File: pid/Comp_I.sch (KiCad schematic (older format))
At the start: 23 parts, among them U10 LM7171, U9 LM7171

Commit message: [pid] -
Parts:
- removed C40, C43: 2n, ~, symbol C
- removed R30, R35: 500, ~, symbol R
- removed R32, R34: 50, ~, symbol R
- added C29: 10u, ~, symbol C
- added C30: 0.01u, ~, symbol C
- added R49: 200k, ~, symbol R
- added R51: 0, ~, symbol R
- added R54: 1M, ~, symbol R
- added R56: 510, ~, symbol R
- added RV14: 100k, ~, symbol POT
- gave numbers to parts that had none: 4
- renumbered C36 to C21, C37 to C22, C38 to C23, C39 to C24, C41 to C27, C42 to C28, R31 to R47, R33 to R50, R36 to R53, R37 to R55, RV3 to RV15, U9 to U5, U10 to U6
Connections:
- net +5V: now also RV14.1
- net -5V: now also RV14.3
- net GND: now also C29.2, C30.1, R54.2
- net Out: now also R56.1
- net at R53.1, U5.6 (Out), U6.2 (-In): now also R51.2
- net Switch_NC/NC renamed Hold/NC
- net Switch_NO/NO renamed Reset1/NO
- net Reset1/NO: now also R49.2, R51.1
- new net: C29.1, R49.1, RV14.2
- new net Reset1/COM: C30.2, R54.1
- new net Reset2/COM: R56.2

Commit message: [pid] -
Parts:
- renumbered R47 to R50, R48 to R51, R49 to R52, R50 to R53, R51 to R54, R52 to R55, R53 to R56, R54 to R57, R55 to R58, R56 to R59
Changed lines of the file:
@@
 $Descr A4 11693 8268
 encoding utf-8
-Sheet 10 47
+Sheet 10 53
 Title ""
-Date "1 may 2014"
+Date "2 may 2014"
 Rev ""
 Comp ""
@@
 	3000 3400 3200 3400
 $Comp
-L R R47
+L R R50
 U 1 1 531FD1A4
 P 4950 3100
-F 0 "R47" V 5030 3100 40  0000 C CNN
+F 0 "R50" V 5030 3100 40  0000 C CNN
 F 1 "100" V 4957 3101 40  0000 C CNN
 F 2 "~" V 4880 3100 30  0000 C CNN
@@
 	7850 3750 7900 3750
 $Comp
-L GND #PWR026
+L GND #PWR031
 U 1 1 531FD1D3
 P 7300 3500
-F 0 "#PWR026" H 7300 3500 30  0001 C CNN
+F 0 "#PWR031" H 7300 3500 30  0001 C CNN
 F 1 "GND" H 7300 3430 30  0001 C CNN
 F 2 "" H 7300 3500 60  0000 C CNN
@@
 	7300 3400 7300 3500
 $Comp
-L R R55
+L R R58
 U 1 1 531FD1DB
 P 8400 2950
-F 0 "R55" V 8480 2950 40  0000 C CNN
+F 0 "R58" V 8480 2950 40  0000 C CNN
 F 1 "200" V 8407 2951 40  0000 C CNN
 F 2 "~" V 8330 2950 30  0000 C CNN
@@
 	8400 2650 8400 2700
 $Comp
-L GND #PWR027
+L GND #PWR032
 U 1 1 531FD1E9
 P 8600 2200
-F 0 "#PWR027" H 8600 2200 30  0001 C CNN
+F 0 "#PWR032" H 8600 2200 30  0001 C CNN
 F 1 "GND" H 8600 2130 30  0001 C CNN
 F 2 "" H 8600 2200 60  0000 C CNN
@@
 $EndComp
 $Comp
-L GND #PWR028
+L GND #PWR033
 U 1 1 531FD20B
 P 2550 1450
-F 0 "#PWR028" H 2550 1450 30  0001 C CNN
+F 0 "#PWR033" H 2550 1450 30  0001 C CNN
 F 1 "GND" H 2550 1380 30  0001 C CNN
 F 2 "" H 2550 1450 60  0000 C CNN
@@
 $Sheet
 S 7400 4050 600  350
-U 5321AFC9
+U 5364DD9B
 F0 "Reset2" 50
 F1 "Switch_NO.sch" 50
@@
 $EndComp
 $Comp
-L GND #PWR029
+L GND #PWR034
 U 1 1 531FF000
 P 5900 4600
-F 0 "#PWR029" H 5900 4600 30  0001 C CNN
+F 0 "#PWR034" H 5900 4600 30  0001 C CNN
 F 1 "GND" H 5900 4530 30  0001 C CNN
 F 2 "" H 5900 4600 60  0000 C CNN
@@
 	7200 3200 7350 3200
 $Comp
-L R R53
+L R R56
 U 1 1 531FF15A
 P 7200 3650
-F 0 "R53" V 7280 3650 40  0000 C CNN
+F 0 "R56" V 7280 3650 40  0000 C CNN
 F 1 "510" V 7207 3651 40  0000 C CNN
 F 2 "~" V 7130 3650 30  0000 C CNN
@@
 	7200 2600 7200 3400
 $Comp
-L R R50
+L R R53
 U 1 1 531FF1DB
 P 6100 3550
-F 0 "R50" V 6180 3550 40  0000 C CNN
+F 0 "R53" V 6180 3550 40  0000 C CNN
 F 1 "10" V 6107 3551 40  0000 C CNN
 F 2 "~" V 6030 3550 30  0000 C CNN
@@
 $EndComp
 $Comp
-L GND #PWR030
+L GND #PWR035
 U 1 1 531FF1E1
 P 6100 4050
-F 0 "#PWR030" H 6100 4050 30  0001 C CNN
+F 0 "#PWR035" H 6100 4050 30  0001 C CNN
 F 1 "GND" H 6100 3980 30  0001 C CNN
 F 2 "" H 6100 4050 60  0000 C CNN
@@
 Connection ~ 5900 4150
 $Comp
-L R R48
+L R R51
 U 1 1 5355E970
 P 5550 3100
-F 0 "R48" V 5630 3100 40  0000 C CNN
+F 0 "R51" V 5630 3100 40  0000 C CNN
 F 1 "10" V 5557 3101 40  0000 C CNN
 F 2 "~" V 5480 3100 30  0000 C CNN
@@
 $EndComp
 $Comp
-L R R52
+L R R55
 U 1 1 5355E9CA
 P 6800 2400
-F 0 "R52" V 6880 2400 40  0000 C CNN
+F 0 "R55" V 6880 2400 40  0000 C CNN
 F 1 "100" V 6807 2401 40  0000 C CNN
 F 2 "~" V 6730 2400 30  0000 C CNN
@@
 Connection ~ 5250 3100
 $Comp
-L GND #PWR031
+L GND #PWR036
 U 1 1 5355EE90
 P 5250 3650
-F 0 "#PWR031" H 5250 3650 30  0001 C CNN
+F 0 "#PWR036" H 5250 3650 30  0001 C CNN
 F 1 "GND" H 5250 3580 30  0001 C CNN
 F 2 "" H 5250 3650 60  0000 C CNN
@@
 $EndComp
 $Comp
-L R R49
+L R R52
 U 1 1 5356CEAF
 P 5900 2150
-F 0 "R49" V 5980 2150 40  0000 C CNN
+F 0 "R52" V 5980 2150 40  0000 C CNN
 F 1 "200k" V 5907 2151 40  0000 C CNN
 F 2 "~" V 5830 2150 30  0000 C CNN
@@
 $EndComp
 $Comp
-L GND #PWR032
+L GND #PWR037
 U 1 1 5356D867
 P 6450 1950
-F 0 "#PWR032" H 6450 1950 30  0001 C CNN
+F 0 "#PWR037" H 6450 1950 30  0001 C CNN
 F 1 "GND" H 6450 1880 30  0001 C CNN
 F 2 "" H 6450 1950 60  0000 C CNN
@@
 	6450 1850 6450 1950
 $Comp
-L R R51
+L R R54
 U 1 1 5358064E
 P 6600 2600
-F 0 "R51" V 6680 2600 40  0000 C CNN
+F 0 "R54" V 6680 2600 40  0000 C CNN
 F 1 "0" V 6607 2601 40  0000 C CNN
 F 2 "~" V 6530 2600 30  0000 C CNN
@@
 $EndComp
 $Comp
-L GND #PWR033
+L GND #PWR038
 U 1 1 535811B7
 P 7050 4900
-F 0 "#PWR033" H 7050 4900 30  0001 C CNN
+F 0 "#PWR038" H 7050 4900 30  0001 C CNN
 F 1 "GND" H 7050 4830 30  0001 C CNN
 F 2 "" H 7050 4900 60  0000 C CNN
@@
 Connection ~ 6200 5000
 $Comp
-L R R56
+L R R59
 U 1 1 535829AC
 P 8400 3700
-F 0 "R56" V 8480 3700 40  0000 C CNN
+F 0 "R59" V 8480 3700 40  0000 C CNN
 F 1 "510" V 8407 3701 40  0000 C CNN
 F 2 "~" V 8330 3700 30  0000 C CNN
@@
 	8400 3950 8400 4150
 $Comp
-L R R54
+L R R57
 U 1 1 53583740
 P 7200 4550
-F 0 "R54" V 7280 4550 40  0000 C CNN
+F 0 "R57" V 7280 4550 40  0000 C CNN
 F 1 "1M" V 7207 4551 40  0000 C CNN
 F 2 "~" V 7130 4550 30  0000 C CNN

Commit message: [pid] layout
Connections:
- net Reset1/COM: now also C27.1, C28.2, R51.2, R52.2, R54.1, U5.3 (+In); no longer C30.2, R57.1
- net Reset1/NO: now also C30.2, R57.1; no longer C27.1, C28.2, R51.2, R52.2, R54.1, U5.3 (+In)
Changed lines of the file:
@@
 Sheet 10 53
 Title ""
-Date "2 may 2014"
+Date "5 may 2014"
 Rev ""
 Comp ""
@@
 	7850 3750 7900 3750
 $Comp
-L GND #PWR42
+L GND #PWR036
 U 1 1 531FD1D3
 P 7300 3500
-F 0 "#PWR42" H 7300 3500 30  0001 C CNN
+F 0 "#PWR036" H 7300 3500 30  0001 C CNN
 F 1 "GND" H 7300 3430 30  0001 C CNN
 F 2 "" H 7300 3500 60  0000 C CNN
@@
 	8400 2650 8400 2700
 $Comp
-L GND #PWR43
+L GND #PWR037
 U 1 1 531FD1E9
 P 8600 2200
-F 0 "#PWR43" H 8600 2200 30  0001 C CNN
+F 0 "#PWR037" H 8600 2200 30  0001 C CNN
 F 1 "GND" H 8600 2130 30  0001 C CNN
 F 2 "" H 8600 2200 60  0000 C CNN
@@
 $EndComp
 $Comp
-L GND #PWR36
+L GND #PWR038
 U 1 1 531FD20B
 P 2550 1450
-F 0 "#PWR36" H 2550 1450 30  0001 C CNN
+F 0 "#PWR038" H 2550 1450 30  0001 C CNN
 F 1 "GND" H 2550 1380 30  0001 C CNN
 F 2 "" H 2550 1450 60  0000 C CNN
@@
 $EndComp
 $Comp
-L GND #PWR38
+L GND #PWR039
 U 1 1 531FF000
 P 5900 4600
-F 0 "#PWR38" H 5900 4600 30  0001 C CNN
+F 0 "#PWR039" H 5900 4600 30  0001 C CNN
 F 1 "GND" H 5900 4530 30  0001 C CNN
 F 2 "" H 5900 4600 60  0000 C CNN
@@
 $EndComp
 $Comp
-L GND #PWR39
+L GND #PWR040
 U 1 1 531FF1E1
 P 6100 4050
-F 0 "#PWR39" H 6100 4050 30  0001 C CNN
+F 0 "#PWR040" H 6100 4050 30  0001 C CNN
 F 1 "GND" H 6100 3980 30  0001 C CNN
 F 2 "" H 6100 4050 60  0000 C CNN
@@
 Connection ~ 5250 3100
 $Comp
-L GND #PWR37
+L GND #PWR041
 U 1 1 5355EE90
 P 5250 3650
-F 0 "#PWR37" H 5250 3650 30  0001 C CNN
+F 0 "#PWR041" H 5250 3650 30  0001 C CNN
 F 1 "GND" H 5250 3580 30  0001 C CNN
 F 2 "" H 5250 3650 60  0000 C CNN
@@
 $EndComp
 $Comp
-L GND #PWR40
+L GND #PWR042
 U 1 1 5356D867
 P 6450 1950
-F 0 "#PWR40" H 6450 1950 30  0001 C CNN
+F 0 "#PWR042" H 6450 1950 30  0001 C CNN
 F 1 "GND" H 6450 1880 30  0001 C CNN
 F 2 "" H 6450 1950 60  0000 C CNN
@@
 F0 "Reset1" 50
 F1 "Switch_NO.sch" 50
-F2 "NO" I L 6300 4150 60
+F2 "NO" I R 6900 4150 60
 F3 "IN" I L 6300 4300 60
-F4 "COM" I R 6900 4150 60
+F4 "COM" I L 6300 4150 60
 $EndSheet
 $Comp
@@
 $EndComp
 $Comp
-L GND #PWR41
+L GND #PWR043
 U 1 1 535811B7
 P 7050 4900
-F 0 "#PWR41" H 7050 4900 30  0001 C CNN
+F 0 "#PWR043" H 7050 4900 30  0001 C CNN
 F 1 "GND" H 7050 4830 30  0001 C CNN
 F 2 "" H 7050 4900 60  0000 C CNN

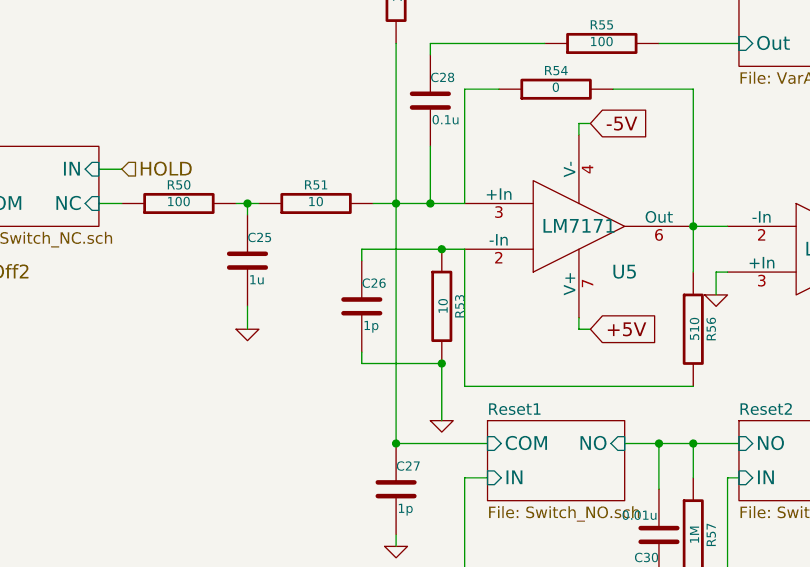
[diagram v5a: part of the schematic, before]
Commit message: [pid] remove high freq bypass capacitor for integrator pre amp
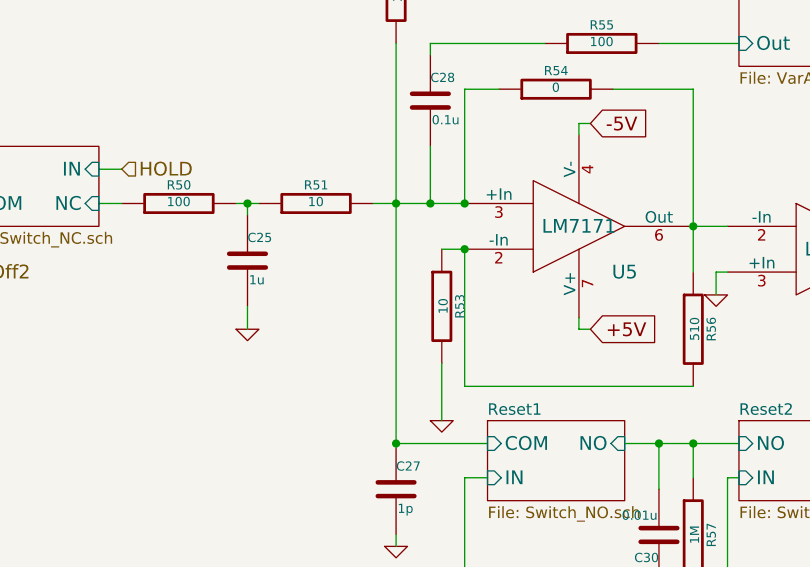
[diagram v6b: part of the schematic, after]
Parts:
- removed C26: 1p, ~, symbol C
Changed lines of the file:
@@
 Sheet 10 53
 Title ""
-Date "5 may 2014"
+Date "19 may 2014"
 Rev ""
 Comp ""
@@
 	6200 3900 6200 3300
 Wire Wire Line
-	6200 3300 5750 3300
-Wire Wire Line
 	6100 3800 6100 4050
 Wire Wire Line
 	8350 3300 8450 3300
 Connection ~ 8400 3300
-$Comp
-L C C26
-U 1 1 53558A6B
-P 5750 3550
-F 0 "C26" H 5750 3650 40  0000 L CNN
-F 1 "1p" H 5756 3465 40  0000 L CNN
-F 2 "~" H 5788 3400 30  0000 C CNN
-F 3 "~" H 5750 3550 60  0000 C CNN
-	1    5750 3550
-	1    0    0    -1
-$EndComp
-Wire Wire Line
-	5750 3300 5750 3350
-Connection ~ 6100 3300
-Wire Wire Line
-	5750 3750 5750 3800
-Wire Wire Line
-	5750 3800 6100 3800
-Connection ~ 6100 3800
 Connection ~ 5900 3100
 Connection ~ 5900 4150
@@
 Wire Wire Line
 	4600 2950 4700 2950
+Wire Wire Line
+	6200 3300 6100 3300
+Connection ~ 6200 3300
+Connection ~ 6200 3100
 $EndSCHEMATC

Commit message: [pid] update
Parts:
- C27: value 1p -> 0(1p)
- C28: value 0.1u -> 0.022u
- C30: value 0.01u -> 10u
- R50: value 100 -> 5k
- R51: value 10 -> 5
- R53: value 10 -> 100
- R54: value 0 -> inf(0)
- R55: value 100 -> 200
- R57: value 1M -> 1k
- R59: value 510 -> 1k
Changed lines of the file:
@@
 Sheet 10 53
 Title ""
-Date "19 may 2014"
+Date "28 may 2014"
 Rev ""
 Comp ""
@@
 P 4950 3100
 F 0 "R50" V 5030 3100 40  0000 C CNN
-F 1 "100" V 4957 3101 40  0000 C CNN
+F 1 "5k" V 4957 3101 40  0000 C CNN
 F 2 "~" V 4880 3100 30  0000 C CNN
 F 3 "~" H 4950 3100 30  0000 C CNN
@@
 F 3 "~" H 7750 3300 60  0000 C CNN
 	1    7750 3300
-	1    0    0    -1
-$EndComp
-$Comp
-L C C28
-U 1 1 531FD1B0
-P 6050 2650
-F 0 "C28" H 6050 2750 40  0000 L CNN
-F 1 "0.1u" H 6056 2565 40  0000 L CNN
-F 2 "~" H 6088 2500 30  0000 C CNN
-F 3 "~" H 6050 2650 60  0000 C CNN
-	1    6050 2650
 	1    0    0    -1
 $EndComp
@@
 P 5900 4350
 F 0 "C27" H 5900 4450 40  0000 L CNN
-F 1 "1p" H 5906 4265 40  0000 L CNN
+F 1 "0(1p)" H 5906 4265 40  0000 L CNN
 F 2 "~" H 5938 4200 30  0000 C CNN
 F 3 "~" H 5900 4350 60  0000 C CNN
@@
 P 6100 3550
 F 0 "R53" V 6180 3550 40  0000 C CNN
-F 1 "10" V 6107 3551 40  0000 C CNN
+F 1 "100" V 6107 3551 40  0000 C CNN
 F 2 "~" V 6030 3550 30  0000 C CNN
 F 3 "~" H 6100 3550 30  0000 C CNN
@@
 P 5550 3100
 F 0 "R51" V 5630 3100 40  0000 C CNN
-F 1 "10" V 5557 3101 40  0000 C CNN
+F 1 "5" V 5557 3101 40  0000 C CNN
 F 2 "~" V 5480 3100 30  0000 C CNN
 F 3 "~" H 5550 3100 30  0000 C CNN
@@
 P 6800 2400
 F 0 "R55" V 6880 2400 40  0000 C CNN
-F 1 "100" V 6807 2401 40  0000 C CNN
+F 1 "200" V 6807 2401 40  0000 C CNN
 F 2 "~" V 6730 2400 30  0000 C CNN
 F 3 "~" H 6800 2400 30  0000 C CNN
@@
 P 6600 2600
 F 0 "R54" V 6680 2600 40  0000 C CNN
-F 1 "0" V 6607 2601 40  0000 C CNN
+F 1 "inf(0)" V 6607 2601 40  0000 C CNN
 F 2 "~" V 6530 2600 30  0000 C CNN
 F 3 "~" H 6600 2600 30  0000 C CNN
@@
 P 7050 4550
 F 0 "C30" H 7050 4650 40  0000 L CNN
-F 1 "0.01u" H 7056 4465 40  0000 L CNN
+F 1 "10u" H 7056 4465 40  0000 L CNN
 F 2 "~" H 7088 4400 30  0000 C CNN
 F 3 "~" H 7050 4550 60  0000 C CNN
@@
 P 8400 3700
 F 0 "R59" V 8480 3700 40  0000 C CNN
-F 1 "510" V 8407 3701 40  0000 C CNN
+F 1 "1k" V 8407 3701 40  0000 C CNN
 F 2 "~" V 8330 3700 30  0000 C CNN
 F 3 "~" H 8400 3700 30  0000 C CNN
@@
 P 7200 4550
 F 0 "R57" V 7280 4550 40  0000 C CNN
-F 1 "1M" V 7207 4551 40  0000 C CNN
+F 1 "1k" V 7207 4551 40  0000 C CNN
 F 2 "~" V 7130 4550 30  0000 C CNN
 F 3 "~" H 7200 4550 30  0000 C CNN
@@
 Connection ~ 6200 3300
 Connection ~ 6200 3100
+$Comp
+L C C28
+U 1 1 531FD1B0
+P 6050 2650
+F 0 "C28" H 6050 2750 40  0000 L CNN
+F 1 "0.022u" H 6056 2565 40  0000 L CNN
+F 2 "~" H 6088 2500 30  0000 C CNN
+F 3 "~" H 6050 2650 60  0000 C CNN
+	1    6050 2650
+	1    0    0    -1
+$EndComp
 $EndSCHEMATC
